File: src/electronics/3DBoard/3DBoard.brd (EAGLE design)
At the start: 139.7 x 110.2 mm, 30 parts, among them IC1 78L05Z, IC10 2987-DRV8825, IC2 2987-DRV8825, IC3 2987-DRV8825, IC4 2987-DRV8825, IC5 2987-DRV8825, IC6 2987-DRV8825, IC7 2987-DRV8825, IC8 2987-DRV8825, IC9 2987-DRV8825

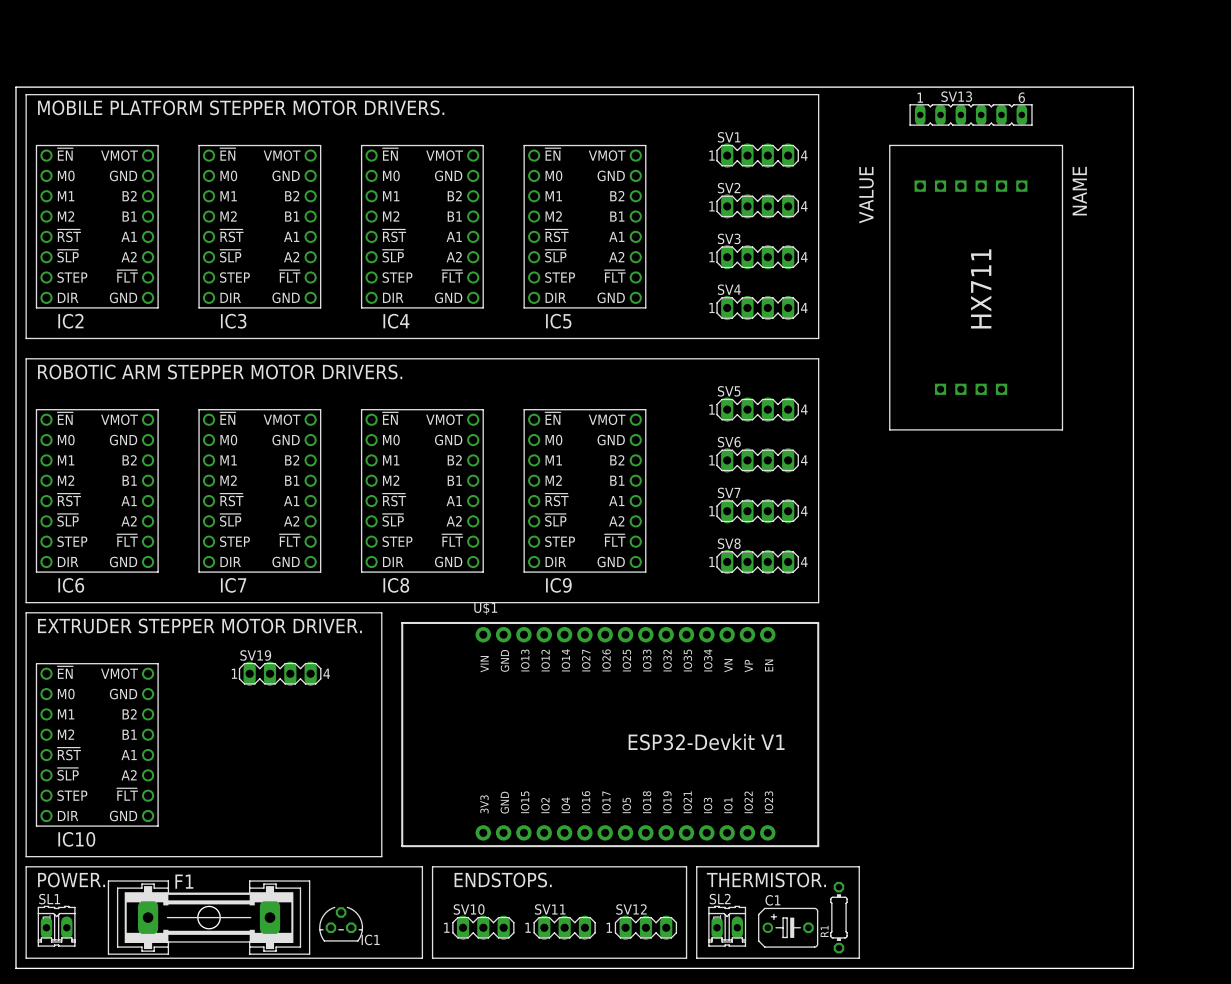
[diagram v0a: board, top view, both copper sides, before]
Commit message: Wiring added and schematics are cleaner.
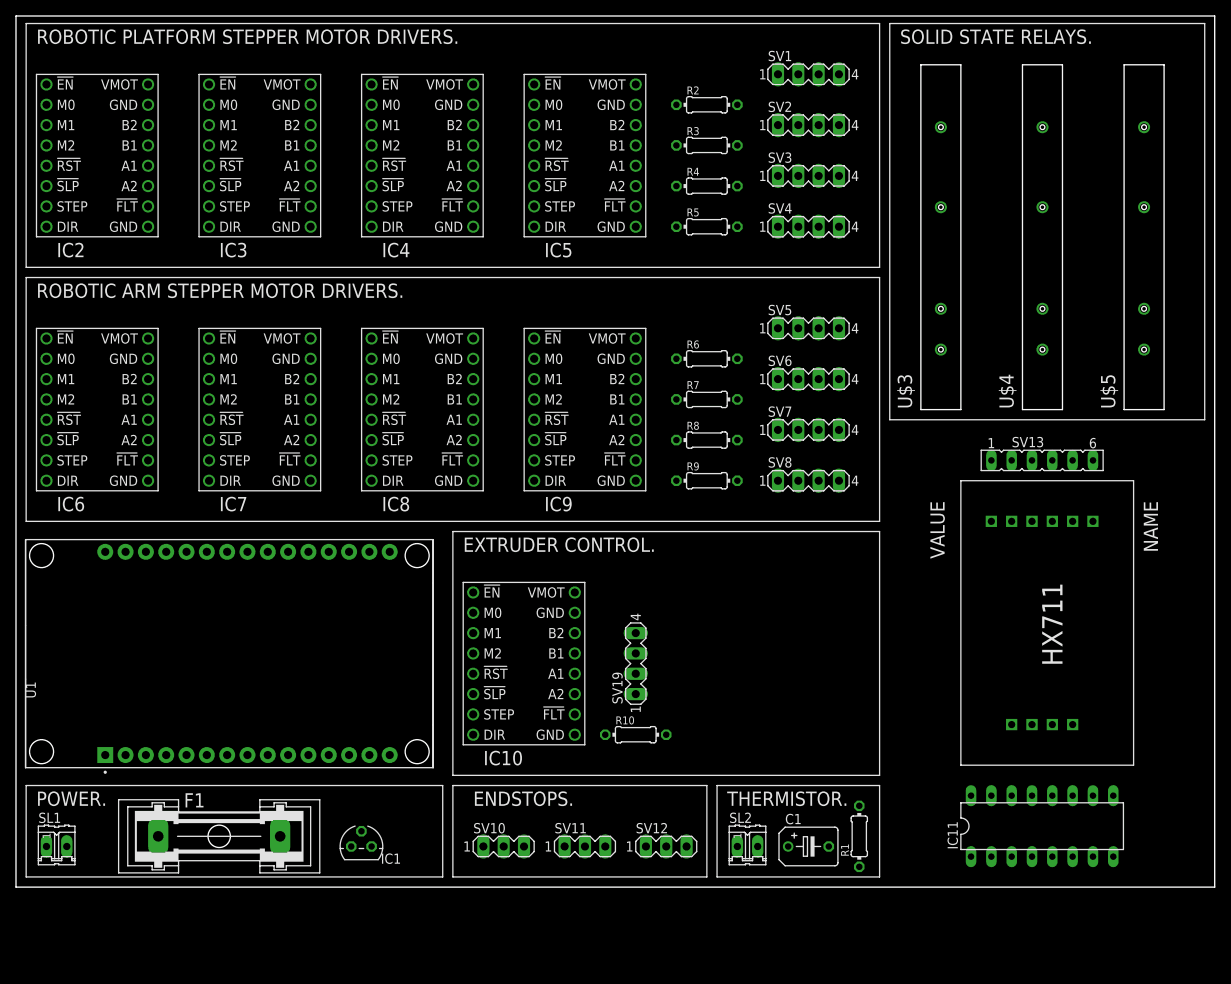
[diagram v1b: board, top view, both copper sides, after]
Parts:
- removed U$1: ESP32DEVKITV1, ESP32-DEVKITV1:ESP32-DEVKITV1
- added IC11: 74S139N, 74xx-us:DIL16
- added R10, R2, R3, R4, R5, R6, R7, R8, R9: 10k, rcl:0204/7
- added U$3, U$4, U$5: CMX60D10, CMX60D10:SIP-4
- added U1: ESP32-DEVKIT-V1, ESP32-DEVKIT-V1:MODULE_ESP32_DEVKIT_V1
- moved IC10 54.3 mm to (63.5, 27.9)
- moved SV19 44.5 mm to (77.5, 27.9), turned to 90 degrees
- moved SV13 44.1 mm to (128.3, 53.3)
- moved U$2 42.8 mm to (105.4, 54.6)
- moved SV3 12.0 mm to (99.1, 88.9)
- moved SV1 12.0 mm to (99.1, 101.6)
- moved SV2 12.0 mm to (99.1, 95.2)
- moved SV4 12.0 mm to (99.1, 82.5)
- moved SV5 12.0 mm to (99.1, 69.8)
- moved SV6 12.0 mm to (99.1, 63.5)
- moved SV7 12.0 mm to (99.1, 57.1)
- moved SV8 12.0 mm to (99.1, 50.8)
- moved C1 10.5 mm to (99.1, 5.08)
- moved IC1 10.5 mm to (43.2, 5.08)
- moved SV10 10.5 mm to (61.0, 5.08)
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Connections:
- removed net GND1: IC10.9
- removed net GND2: IC6.15
- removed net N$34 (its old number): F1.2, IC1.3, IC10.16, IC2.16, IC3.16, IC4.16, IC5.16, IC6.16, IC7.16, IC8.16, IC9.16, U$1.30
- removed net N$35 (its old number): C1.-, IC1.2, IC10.15, IC2.15, IC3.15, IC4.15, IC5.15, IC7.15, IC8.15, IC9.15, SL1.1, SL2.1, SV10.2, SV11.2, SV12.2, U$1.28, U$2.GND
- removed net N$47 (its old number): F1.1, SL1.2
- removed net N$48: C1.+, R1.1, SL2.2
- new net GND: IC11.8
- new net N$2: IC10.16, U$5.+DCLOAD
- new net N$3: IC6.16, IC7.16, IC8.16, IC9.16, U$4.+DCLOAD
- new net N$4: IC2.16, IC3.16, IC4.16, IC5.16, U$3.+DCLOAD
- new net N$46: F1.1, SL1.1
- new net N$53: IC3.8, U1.8
- new net N$54: IC3.7, U1.27
- new net N$55: IC4.8, U1.28
- new net N$56: IC4.7, U1.26
- new net N$57: IC5.8, U1.3
- new net N$58: IC2.5, IC2.6
- new net N$59: IC3.5, IC3.6
- new net N$6: IC2.7, U1.5
- new net N$60: IC4.5, IC4.6
- new net N$61: IC5.5, IC5.6
- new net N$62: IC6.5, IC6.6
- new net N$63: IC7.5, IC7.6
- new net N$64: IC8.5, IC8.6
- new net N$65: IC9.5, IC9.6
- new net N$66: IC10.5, IC10.6
- new net N$67: IC2.1, R2.2
- new net N$68: IC3.1, R3.2
- new net N$69: IC4.1, R4.2
- new net N$70: IC5.1, R5.2
- new net N$71: IC7.1, R6.2
- new net N$72: IC8.1, R7.2
- new net N$73: IC9.1, R8.2
- new net N$74: IC10.1, R9.2
- new net N$75: IC6.1, R10.2
- new net N$76: IC5.7, U1.9
- new net N$77: IC6.8, U1.10
- new net N$78: F1.2, IC1.3, U$3.-DCLOAD, U$4.-DCLOAD, U$5.-DCLOAD, U1.30
- new net N$79: IC1.1, IC10.2, IC10.3, IC10.4, IC2.2, IC2.3, IC2.4, IC3.2, IC3.3, IC3.4, IC4.2, IC4.3, IC4.4, IC5.2, IC5.3, IC5.4, IC6.2, IC6.3, IC6.4, IC7.2, IC7.3, IC7.4, IC8.2, IC8.3, IC8.4, IC9.2, IC9.3, IC9.4, R1.2, R10.1, R2.1, R3.1, R4.1, R5.1, R6.1, R7.1, R8.1, R9.1, SV10.3, SV11.3, SV12.3, U$2.VCC
- new net N$80: IC6.7, U1.11
- new net N$81: IC7.8, U1.14
- new net N$82: IC7.7, U1.15
- new net N$83: IC8.8, U1.23
- new net N$84: IC8.7, U1.24
- new net N$85: IC9.8, U1.25
- new net N$86: IC9.7, U1.21
- new net N$87: IC11.6, U$5.+DCCONTROL
- new net N$88: IC10.7, U1.13
- new net N$89: IC11.4, U$3.+DCCONTROL
- new net N$90: IC11.5, U$4.+DCCONTROL
- new net N$91: SV10.1, U1.20
- new net N$92: SV11.1, U1.19
- new net N$93: IC10.8, U1.12
- new net N$94: C1.+, R1.1, SL2.2, U1.17
- new net N$95: IC11.2, U1.6
- new net N$96: IC11.3, U1.7
- new net N$97: SV12.1, U1.18
- new net VCC: IC11.16
- net N$1: now also IC2.8, U1.4; no longer IC2.9, IC3.9, IC4.9, IC5.9, IC6.9, IC7.9, IC8.9, IC9.9, U$1.2
- net N$43: now also C1.-, IC1.2, IC10.15, IC10.9, IC2.15, IC2.9, IC3.15, IC3.9, IC4.15, IC4.9, IC5.15, IC5.9, IC6.15, IC6.9, IC7.15, IC7.9, IC8.15, IC8.9, IC9.15, IC9.9, SL1.2, SL2.1, SV10.2, SV11.2, SV12.2, U$2.GND, U$3.-DCCONTROL, U$4.-DCCONTROL, U$5.-DCCONTROL, U1.2, U1.29; no longer IC1.1, R1.2, SV10.3, SV11.3, SV12.3, U$2.VCC
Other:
- board size 139.7 x 110.2 mm -> 149.8 x 108.9 mm
- board text added: "EXTRUDER CONTROL."
- board text added: "ROBOTIC PLATFORM STEPPER MOTOR DRIVERS."
- board text added: "SOLID STATE RELAYS."
- board text removed: "EXTRUDER STEPPER MOTOR DRIVER."
- board text removed: "MOBILE PLATFORM STEPPER MOTOR DRIVERS."
